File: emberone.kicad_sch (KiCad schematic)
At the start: 18 parts, among them J1 Screw Terminal, J2 Screw Terminal

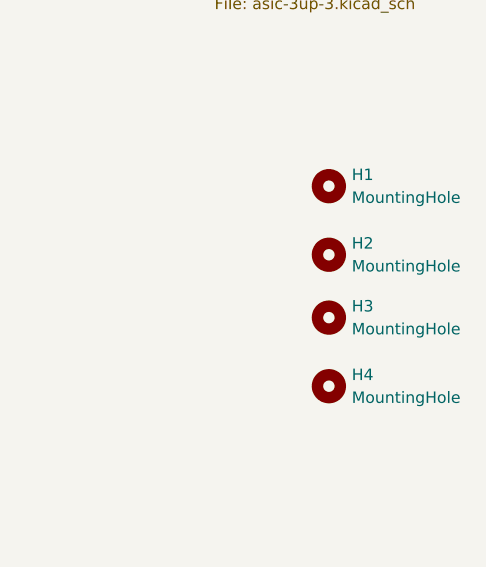
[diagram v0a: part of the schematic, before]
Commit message: fixup fiducials for #49
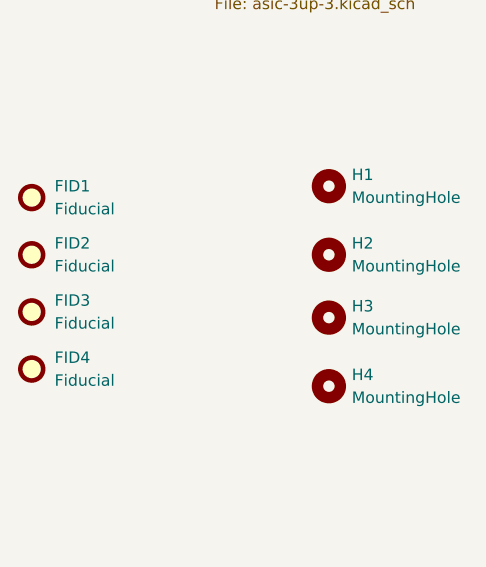
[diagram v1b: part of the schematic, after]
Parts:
- added FID1, FID2, FID3, FID4: Fiducial, emberone:Fiducial_1mm_Mask2mm, symbol Mechanical:Fiducial
